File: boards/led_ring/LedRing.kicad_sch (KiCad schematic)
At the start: 35 parts, among them J10 FH12-10S-0.5SH(55)

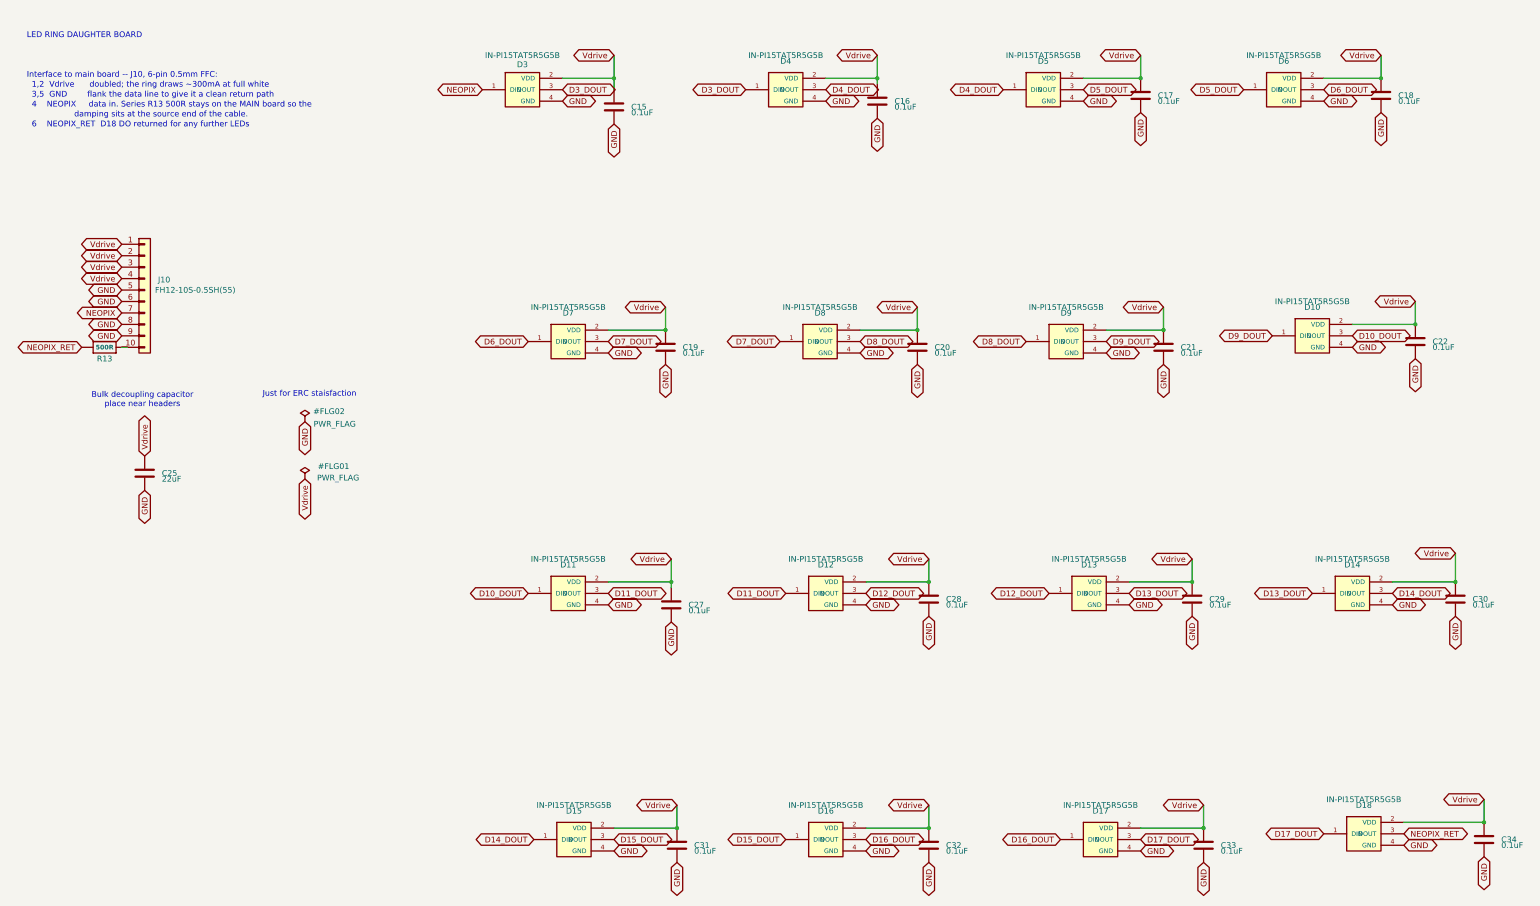
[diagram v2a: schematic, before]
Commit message: Add a voltage booster and logic shift to the LED ring. Power consumption implications, but necessary
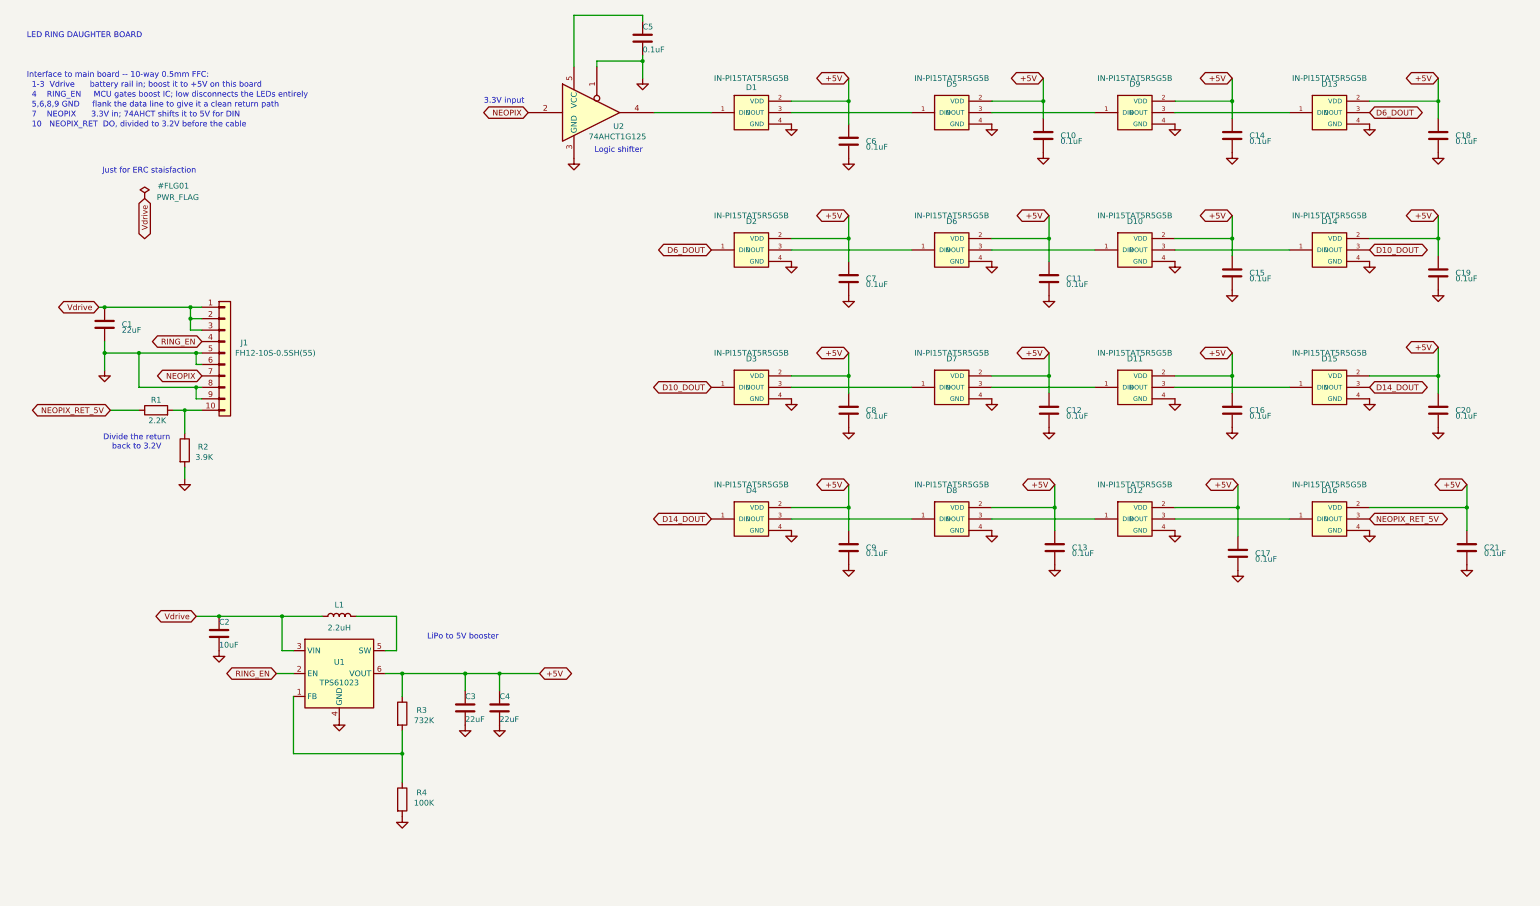
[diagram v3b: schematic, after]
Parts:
- removed R13: 500R, Resistor_SMD:R_0603_1608Metric, symbol smart_compass_main:RESISTOR_0603_NOOUT
- added C2: 10uF, Capacitor_SMD:C_0805_2012Metric, symbol Device:C
- added C3, C4: 22uF, Capacitor_SMD:C_0805_2012Metric, symbol Device:C
- added C5: 0.1uF, Capacitor_SMD:C_0402_1005Metric, symbol Device:C
- added L1: 2.2uH, Inductor_SMD:L_1008_2520Metric, symbol Device:L
- added R1: 2.2K, Resistor_SMD:R_0603_1608Metric, symbol Device:R
- added R2: 3.9K, Resistor_SMD:R_0603_1608Metric, symbol Device:R
- added R3: 732K, Resistor_SMD:R_0603_1608Metric, symbol Device:R
- added R4: 100K, Resistor_SMD:R_0603_1608Metric, symbol Device:R
- added U1: TPS61023, Package_TO_SOT_SMD:SOT-563, symbol smart_compass:TPS61023
- added U2: 74AHCT1G125, Package_TO_SOT_SMD:SOT-23-5, symbol 74xGxx:74AHCT1G125
- D1: renamed from D3; Sourcing_Note V_IH is specified as 3.4V absolute at VDD=5.0V, NOT as a ra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 -> Run at VDD = 5.0V from the on-board boost U9, which is the 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
- J1: renamed from J10; Sourcing_Note The four spare ways double up the supply and return: Vdrive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 -> Vdrive on 1-3, RING_EN on 4, GND on 5, 6, 8, 9, NEOPIX on 7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
- renumbered C25 to C1, C16 to C10, C20 to C11, C28 to C12, C32 to C13, C17 to C14, C21 to C15, C29 to C16, C33 to C17, C22 to C19, C30 to C20, C34 to C21, C15 to C6, C19 to C7, C27 to C8, C31 to C9, D9 to D10, D13 to D11, D17 to D12, D6 to D13, D10 to D14, D14 to D15, D18 to D16, D7 to D2, D11 to D3, D15 to D4, D4 to D5, D8 to D6, D12 to D7, D16 to D8, D5 to D9
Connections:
- net GND: now also C2.2, C3.2, C4.2, C5.2, R2.2, R4.2, U1.4 (GND), U2.1, U2.3 (GND)
- net NEOPIX: now also U2.2; no longer D1.1 (DIN)
- net Vdrive: now also C2.1, L1.1, U1.3 (VIN); no longer C10.1, C11.1, C12.1, C13.1, C14.1, C15.1, C16.1, C17.1, C18.1, C19.1, C20.1, C21.1, C6.1, C7.1, C8.1, C9.1, D1.2 (VDD), D10.2 (VDD), D11.2 (VDD), D12.2 (VDD), D13.2 (VDD), D14.2 (VDD), D15.2 (VDD), D16.2 (VDD), D2.2 (VDD), D3.2 (VDD), D4.2 (VDD), D5.2 (VDD), D6.2 (VDD), D7.2 (VDD), D8.2 (VDD), D9.2 (VDD), J1.4 (Pin_4)
- net at J1.10 (Pin_10): now also R1.2, R2.1
- net D11_DOUT: no longer names the net of D3.3 (DOUT), D7.1 (DIN)
- net D12_DOUT: no longer names the net of D11.1 (DIN), D7.3 (DOUT)
- net D13_DOUT: no longer names the net of D11.3 (DOUT), D15.1 (DIN)
- net D15_DOUT: no longer names the net of D4.3 (DOUT), D8.1 (DIN)
- net D16_DOUT: no longer names the net of D12.1 (DIN), D8.3 (DOUT)
- net D17_DOUT: no longer names the net of D12.3 (DOUT), D16.1 (DIN)
- net D3_DOUT: no longer names the net of D1.3 (DOUT), D5.1 (DIN)
- net D4_DOUT: no longer names the net of D5.3 (DOUT), D9.1 (DIN)
- net D5_DOUT: no longer names the net of D13.1 (DIN), D9.3 (DOUT)
- net D7_DOUT: no longer names the net of D2.3 (DOUT), D6.1 (DIN)
- net D8_DOUT: no longer names the net of D10.1 (DIN), D6.3 (DOUT)
- net D9_DOUT: no longer names the net of D10.3 (DOUT), D14.1 (DIN)
- net NEOPIX_RET renamed NEOPIX_RET_5V
- net NEOPIX_RET_5V: now also R1.1
- new net: D1.1 (DIN), U2.4
- new net: L1.2, U1.5 (SW)
- new net: R3.2, R4.1, U1.1 (FB)
- new net: C5.1, U2.5 (VCC)
- new net +5V: C10.1, C11.1, C12.1, C13.1, C14.1, C15.1, C16.1, C17.1, C18.1, C19.1, C20.1, C21.1, C3.1, C4.1, C6.1, C7.1, C8.1, C9.1, D1.2 (VDD), D10.2 (VDD), D11.2 (VDD), D12.2 (VDD), D13.2 (VDD), D14.2 (VDD), D15.2 (VDD), D16.2 (VDD), D2.2 (VDD), D3.2 (VDD), D4.2 (VDD), D5.2 (VDD), D6.2 (VDD), D7.2 (VDD), D8.2 (VDD), D9.2 (VDD), R3.1, U1.6 (VOUT)
- new net RING_EN: J1.4 (Pin_4), U1.2 (EN)
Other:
- note added: "1-3 Vdrive battery rail in; boost it to +5V on this board"
- note added: "10 NEOPIX_RET DO, divided to 3.2V before the cable"
- note added: "3.3V input"
- note added: "4 RING_EN MCU gates boost IC; low disconnects the LEDs entirely"
- note added: "5,6,8,9 GND flank the data line to give it a clean return path"
- note added: "7 NEOPIX 3.3V in; 74AHCT shifts it to 5V for DIN"
- note added: "Divide the return back to 3.2V"
- note added: "Interface to main board -- 10-way 0.5mm FFC:"
- note added: "LiPo to 5V booster"
- note added: "Logic shifter"
- note removed: "1,2 Vdrive doubled; the ring draws ~300mA at full white"
- note removed: "3,5 GND flank the data line to give it a clean return path"
- note removed: "4 NEOPIX data in. Series R13 500R stays on the MAIN board so the"
- note removed: "6 NEOPIX_RET D18 DO returned for any further LEDs"
- note removed: "Bulk decoupling capacitor place near headers"
- note removed: "Interface to main board -- J10, 6-pin 0.5mm FFC:"
- note removed: "damping sits at the source end of the cable."
- moved on the sheet: C1, C10, C11, C12, C13, C14, C15, C16, C17, C18, C19, C20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

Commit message: Going down the todo list. Slowed the charge speed
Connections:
- net +5V: now also C5.1, U2.5 (VCC)
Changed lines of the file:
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@@
 	)
 	(junction
+		(at 143.51 17.78)
+		(diameter 0)
+		(color 0 0 0 0)
+	)
+	(junction
 		(at 127 163.83)
 		(diameter 0)
@@
 	(wire
 		(pts
+			(xy 135.89 17.78) (xy 143.51 17.78)
+		)
+		(stroke
+			(width 0)
+			(type default)
+		)
+	)
+	(wire
+		(pts
 			(xy 158.75 17.78) (xy 158.75 19.05)
 		)
@@
 			(hide yes)
 			(show_name no)
+			(do_not_autoplace no)
+			(effects
+				(font
+					(size 1.27 1.27)
+				)
+			)
+		)
+	)
+	(global_label "+5V"
+		(shape bidirectional)
+		(at 135.89 17.78 180)
+		(effects
+			(font
+				(size 1.27 1.27)
+			)
+			(justify right)
+		)
+		(property "Intersheetrefs" "${INTERSHEET_REFS}"
+			(at 135.89 17.78 0)
+			(hide yes)
+			(show_name no)

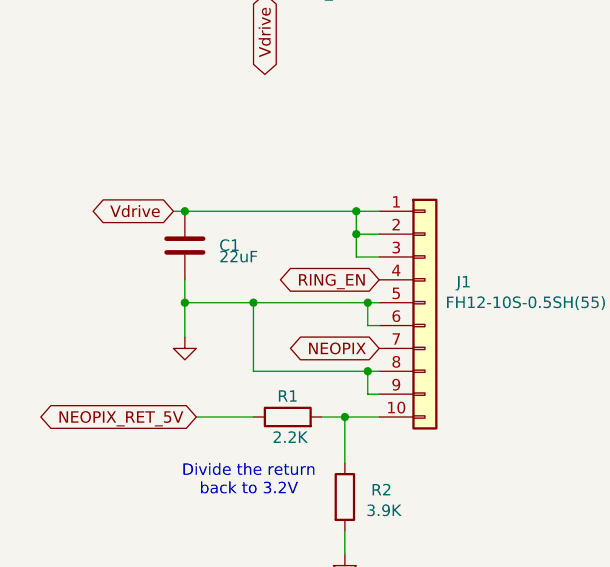
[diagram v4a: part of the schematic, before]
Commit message: and power flag to the led ring ground label
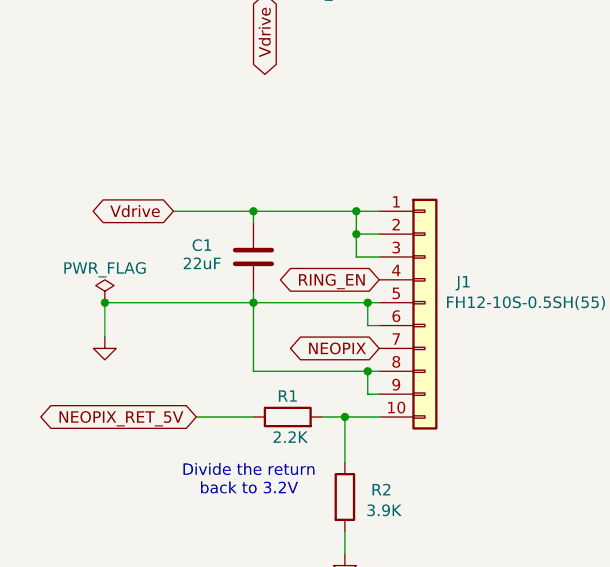
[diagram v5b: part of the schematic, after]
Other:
- moved on the sheet: C1
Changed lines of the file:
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@@
 	)
 	(junction
-		(at 39.37 82.55)
-		(diameter 0)
-		(color 0 0 0 0)
-	)
-	(junction
 		(at 248.92 67.31)
 		(diameter 0)
@@
 	)
 	(junction
-		(at 39.37 92.71)
-		(diameter 0)
-		(color 0 0 0 0)
-	)
-	(junction
 		(at 335.28 97.79)
 		(diameter 0)
@@
 	)
 	(junction
+		(at 30.48 92.71)
+		(diameter 0)
+		(color 0 0 0 0)
+	)
+	(junction
 		(at 105.41 181.61)
 		(diameter 0)
@@
 	)
 	(junction
+		(at 46.99 82.55)
+		(diameter 0)
+		(color 0 0 0 0)
+	)
+	(junction
 		(at 59.69 92.71)
 		(diameter 0)
@@
 	(wire
 		(pts
-			(xy 39.37 92.71) (xy 46.99 92.71)
+			(xy 143.51 17.78) (xy 143.51 29.21)
 		)
 		(stroke
@@
 	(wire
 		(pts
-			(xy 143.51 17.78) (xy 143.51 29.21)
+			(xy 30.48 92.71) (xy 46.99 92.71)
 		)
 		(stroke
@@
 	(wire
 		(pts
-			(xy 39.37 82.55) (xy 58.42 82.55)
-		)
-		(stroke
-			(width 0)
-			(type default)
-		)
-	)
-	(wire
-		(pts
 			(xy 247.65 31.75) (xy 247.65 36.83)
 		)
@@
 	(wire
 		(pts
+			(xy 46.99 82.55) (xy 58.42 82.55)
+		)
+		(stroke
+			(width 0)
+			(type default)
+		)
+	)
+	(wire
+		(pts
 			(xy 290.83 121.92) (xy 290.83 127)
 		)
@@
 	(wire
 		(pts
+			(xy 46.99 83.82) (xy 46.99 82.55)
+		)
+		(stroke
+			(width 0)
+			(type default)
+		)
+	)
+	(wire
+		(pts
 			(xy 204.47 67.31) (xy 191.77 67.31)
 		)
@@
 	(wire
 		(pts
-			(xy 39.37 96.52) (xy 39.37 92.71)
+			(xy 30.48 96.52) (xy 30.48 92.71)
 		)
 		(stroke
@@
 	(wire
 		(pts
-			(xy 39.37 92.71) (xy 39.37 90.17)
+			(xy 46.99 92.71) (xy 46.99 91.44)
 		)
 		(stroke
@@
 	(wire
 		(pts
-			(xy 38.1 82.55) (xy 39.37 82.55)
+			(xy 38.1 82.55) (xy 46.99 82.55)
 		)
 		(stroke
@@
 	(symbol
 		(lib_id "Device:C")
-		(at 39.37 86.36 0)
+		(at 46.99 87.63 0)
 		(unit 1)
 		(body_style 1)
@@
 		(dnp no)
 		(property "Reference" "C1"
-			(at 43.18 86.36 0)
+			(at 40.132 86.36 0)
 			(show_name no)
 			(do_not_autoplace no)
@@
 		)
 		(property "Value" "22uF"
-			(at 43.18 87.63 0)
+			(at 39.116 88.392 0)
 			(show_name no)
 			(do_not_autoplace no)
@@
 		)
 		(property "Footprint" "Capacitor_SMD:C_0805_2012Metric"
-			(at 40.335 82.55 0)
+			(at 47.955 83.82 0)
 			(hide yes)
 			(show_name no)
@@
 		)
 		(property "Datasheet" ""
-			(at 39.37 86.36 0)
+			(at 46.99 87.63 0)
 			(hide yes)
 			(show_name no)
@@
 		)
 		(property "Description" "Ring bulk capacitance, sited at the load end of the FFC so the cable inductance is not in the path. The per-LED 0.1uF parts handle the fast edges."
-			(at 39.37 86.36 0)
+			(at 46.99 87.63 0)
 			(hide yes)
 			(show_name no)
@@
 		)
 		(property "MPN" "CL21A226KPCLRNC"
-			(at 39.37 86.36 0)
+			(at 46.99 87.63 0)
 			(hide yes)
 			(show_name no)
@@
 		)
 		(property "Manufacturer" "Samsung Electro-Mechanics"
-			(at 39.37 86.36 0)
+			(at 46.99 87.63 0)
 			(hide yes)
 			(show_name no)
@@
 		)
 		(property "DigiKey_PN" "1276-6786-1-ND"
-			(at 39.37 86.36 0)
+			(at 46.99 87.63 0)
 			(hide yes)
 			(show_name no)
@@
 		)
 		(property "Voltage" "10V"
-			(at 39.37 86.36 0)
+			(at 46.99 87.63 0)
 			(hide yes)
 			(show_name no)
@@
 		)
 		(property "Dielectric" "X5R"
-			(at 39.37 86.36 0)
+			(at 46.99 87.63 0)
 			(hide yes)
 			(show_name no)
@@
 	(symbol
 		(lib_id "power:GND")
-		(at 39.37 96.52 0)
+		(at 30.48 96.52 0)
 		(unit 1)
 		(body_style 1)
@@
 		(fields_autoplaced yes)
 		(property "Reference" "#PWR01"
-			(at 39.37 102.87 0)
+			(at 30.48 102.87 0)
 			(hide yes)
 			(show_name no)
@@
 		)
 		(property "Value" "GND"
-			(at 39.37 101.6 0)
+			(at 30.48 101.6 0)
 			(hide yes)
 			(show_name no)
@@
 		)
 		(property "Footprint" ""
-			(at 39.37 96.52 0)
+			(at 30.48 96.52 0)
 			(hide yes)
 			(show_name no)
@@
 		)
 		(property "Datasheet" ""
-			(at 39.37 96.52 0)
+			(at 30.48 96.52 0)
 			(hide yes)
 			(show_name no)
@@
 		)
 		(property "Description" "Power symbol creates a global label with name \"GND\" , ground"
-			(at 39.37 96.52 0)
+			(at 30.48 96.52 0)
 			(hide yes)
 			(show_name no)
@@
 					(unit 1)
 				)
+			)
+		)
+	)
+	(symbol
+		(lib_id "power:PWR_FLAG")
+		(at 30.48 92.71 0)
+		(unit 1)
+		(body_style 1)
+		(exclude_from_sim no)
+		(in_bom yes)
+		(on_board yes)
+		(in_pos_files yes)
+		(dnp no)
+		(property "Reference" "#FLG02"
+			(at 30.48 94.615 0)
+			(hide yes)
+			(show_name no)
+			(do_not_autoplace no)
+			(effects
+				(font
+					(size 1.27 1.27)
+				)
+			)
+		)
+		(property "Value" "PWR_FLAG"
+			(at 30.48 88.9 0)
+			(show_name no)
+			(do_not_autoplace no)
+			(effects
+				(font
+					(size 1.27 1.27)
+				)
+			)
+		)
+		(property "Footprint" ""
+			(at 30.48 92.71 0)
+			(hide yes)
+			(show_name no)
+			(do_not_autoplace no)
+			(effects
+				(font
+					(size 1.27 1.27)
+				)
+			)
+		)
+		(property "Datasheet" ""
+			(at 30.48 92.71 0)
+			(hide yes)
+			(show_name no)
+			(do_not_autoplace no)
+			(effects
+				(font
+					(size 1.27 1.27)
+				)
+			)
+		)
+		(property "Description" "Special symbol for telling ERC where power comes from"
+			(at 30.48 92.71 0)
+			(hide yes)
+			(show_name no)
+			(do_not_autoplace no)
+			(effects
+				(font
+					(size 1.27 1.27)
+				)
+			)
+		)
+		(pin "1"
+		)
+		(instances
+			(project "LedRing"
+				(path "/c069d6e6-059e-4cea-be19-739e18ba373e"
+					(reference "#FLG02")
+					(unit 1)
+				)

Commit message: Update inductors. However, one still needs a footprint
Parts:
- L1: Sourcing_Note Peak inductor current is about 0.68A at 250mA of LED load from a 3.3V cell, against Isat 3.1A - ample. The 1.0mm height suits the medallion. LAYOUT: the footprint is the generic Inductor_SMD:L_1008_2520Metric land; check the pad geometry against the Murata drawing before committing, the outline matches but the pads are not guaranteed identical. -> Peak inductor current is about 0.68A at 250mA of LED load from a 3.3V cell, against Isat 3.1A - ample. 1.0mm height
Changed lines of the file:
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@@
 			)
 		)
-		(property "Sourcing_Note" "Peak inductor current is about 0.68A at 250mA of LED load from a 3.3V cell, against Isat 3.1A - ample. The 1.0mm height suits the medallion. LAYOUT: the footprint is the generic Inductor_SMD:L_1008_2520Metric land; check the pad geometry against the Murata drawing before committing, the outline matches but the pads are not guaranteed identical."
+		(property "Sourcing_Note" "Peak inductor current is about 0.68A at 250mA of LED load from a 3.3V cell, against Isat 3.1A - ample. 1.0mm height "
 			(at 91.44 151.13 0)
 			(hide yes)
